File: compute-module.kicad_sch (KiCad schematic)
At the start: 99 parts, among them J1 DF40HC(3.0)-100DS-0.4v, J2 DF40HC(3.0)-100DS-0.4v, M1 compute-module-4-1.5mm

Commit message: [#54617] Review requested changes
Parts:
- removed R? (x4): 4x0R_0402_array, antmicro-footprints:4x0R_0402_array_EXB28V, symbol antmicroResistorNetworksArrays:4x0R_0402_array
- added R? (x15): R_0R_0402, antmicro-footprints:R_0402_1005Metric, symbol antmicroResistors0402:R_0R_0402
- added R?: R_100k_0402, antmicro-footprints:R_0402_1005Metric, symbol antmicroResistors0402:R_100k_0402
- D? (x2): MPN TPD1E0B04DPYR -> TPD1E0B04DPYR
- Q? (x2): Manufacturer Panjit -> PANJIT
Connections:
- net Exp.SCL: now also R?.2
- net Exp.SDA: now also R?.2
- net FT4233.SCL: now also R?.2
- net FT4233.SDA: now also R?.2
- net GND: now also R?.1; no longer J1.100, TP?.1
- net I_{2}C_CSI0.SCL: now also R?.2
- net I_{2}C_CSI0.SDA: now also R?.2
- net I_{2}C_LED.SCL: now also R?.2
- net I_{2}C_LED.SDA: now also R?.2
- net I_{2}C_Sensor.SCL: now also R?.2
- net I_{2}C_Sensor.SDA: now also R?.2
- net I_{2}C_{3V3}.SCL: now also R?.1, R?.1, R?.1, R?.1, R?.1, R?.1, R?.1
- net I_{2}C_{3V3}.SDA: now also R?.1, R?.1, R?.1, R?.1, R?.1, R?.1, R?.1
- net NFC.I_{2}C_SCL: now also R?.2
- net NFC.I_{2}C_SDA: now also R?.2
- net PolarfireID: now also R?.2
- net AntmUD.DIM renamed GPIO.18
- net GPIO.18: now also R?.2
- net AntmUD.EN renamed DSICtrl.EN
- net AntmUD.GPIO renamed DSICtrl.GPIO
- net AntmUD.IRQ1 renamed DSICtrl.IRQ1
- net AntmUD.~{IRQ2} renamed DSICtrl.~{IRQ2}
- net AntmUD.~{RST} renamed DSICtrl.~{RST}
- net NVMe.RX_N renamed NVMe.RX0_N
- net NVMe.RX_P renamed NVMe.RX0_P
- net NVMe.TX_N renamed NVMe.TX0_N
- net NVMe.TX_P renamed NVMe.TX0_P
- new net DSICtrl.DIM: R?.1
- new net DSICtrl.SCL: R?.2
- new net DSICtrl.SDA: R?.2
- new net nEXTRST: J1.100, TP?.1
- no-connect marks 16 -> 12
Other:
- note added: "Note: I_{2}C address selection: A2|A1|A0| write address 0 |0 |0 | 0x40 0 |0 |1 | 0x42 0 |1 |0 | 0x44 0 |1 |1 | 0x46 1 |0 |0 | 0x48 1 |0 |1 | 0x4A 1 |1 |0 | 0x4C 1 |1 |1 | 0x4E"
- note removed: "Note: I_{2}C address selection: A2|A1|A0| write address 0 |0 |0 | 0x40 0 |0 |1 | 0x41 0 |1 |0 | 0x42 0 |1 |1 | 0x43 1 |0 |0 | 0x44 1 |0 |1 | 0x45 1 |1 |0 | 0x46 1 |1 |1 | 0x47"
- moved on the sheet: R?

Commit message: [#54617] Re-enumerate reference designators
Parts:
- gave numbers to parts that had none: 104
- renumbered J1 to J201, J2 to J202, M1 to M201, SP1 to SP201, SP2 to SP202, SP3 to SP203, SP4 to SP204
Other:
- moved on the sheet: R238, R239

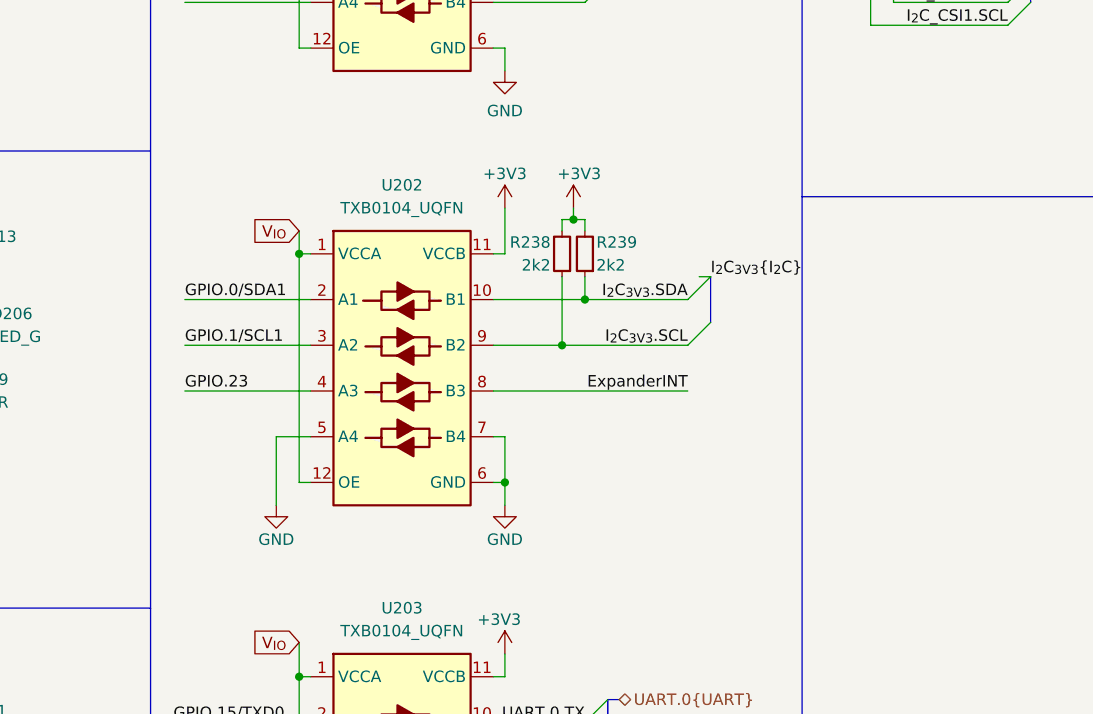
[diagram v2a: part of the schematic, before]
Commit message: [#54617] Change level shifter for I2C
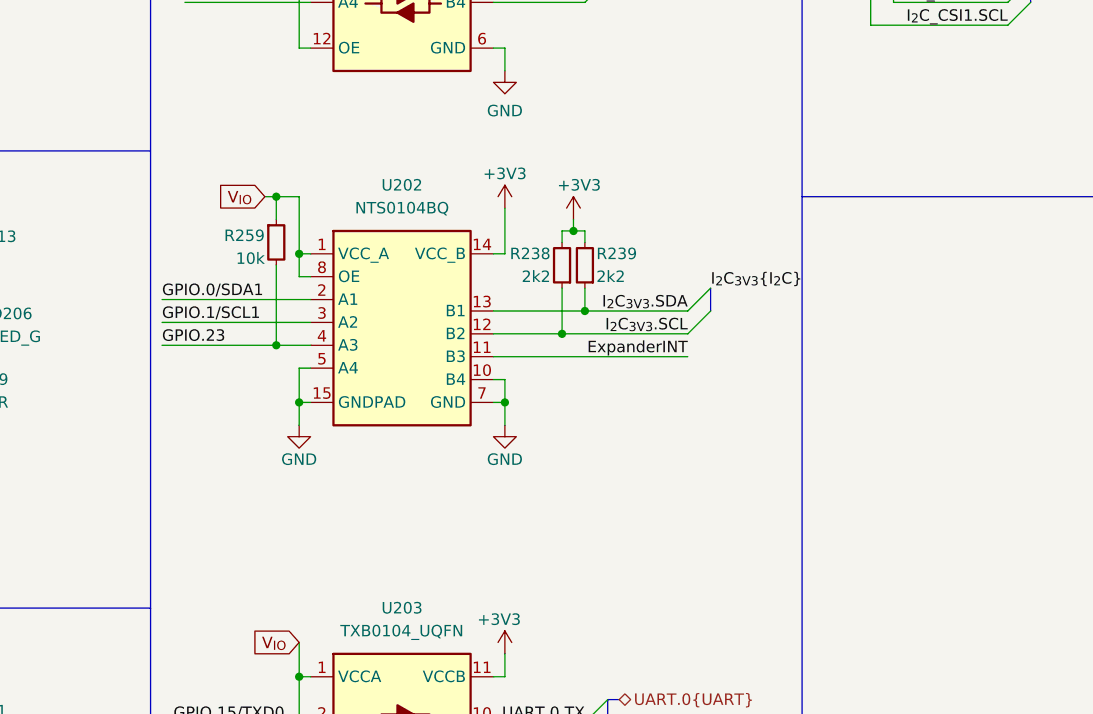
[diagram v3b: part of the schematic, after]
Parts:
- removed U202: TXB0104_UQFN, antmicro-footprints:UQFN-12_2x1.7mm_P0.4mm_Texas_RUT, symbol antmicroLogicTranslatorsLevelShifters:TXB0104_UQFN
- added R259: R_10k_0402, antmicro-footprints:R_0402_1005Metric, symbol antmicroResistors0402:R_10k_0402
- added U202: NTS0104_DHVQFN, antmicro-footprints:DHVQFN-14-1EP_2.5x3mm, symbol antmicroLogicTranslatorsLevelShifters:NTS0104_DHVQFN
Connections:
- net +3V3: now also U202.14 (VCC_B)
- net ExpanderINT: now also U202.11 (B3)
- net GND: now also U202.10 (B4), U202.15 (GNDPAD), U202.5 (A4), U202.7 (GND)
- net GPIO.0/SDA1: now also U202.2 (A1)
- net GPIO.1/SCL1: now also U202.3 (A2)
- net GPIO.23: now also R259.2, U202.4 (A3)
- net I_{2}C_{3V3}.SCL: now also U202.12 (B2)
- net I_{2}C_{3V3}.SDA: now also U202.13 (B1)
- net V_{IO}: now also R259.1, U202.1 (VCC_A), U202.8 (OE)
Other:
- moved on the sheet: R238, R239

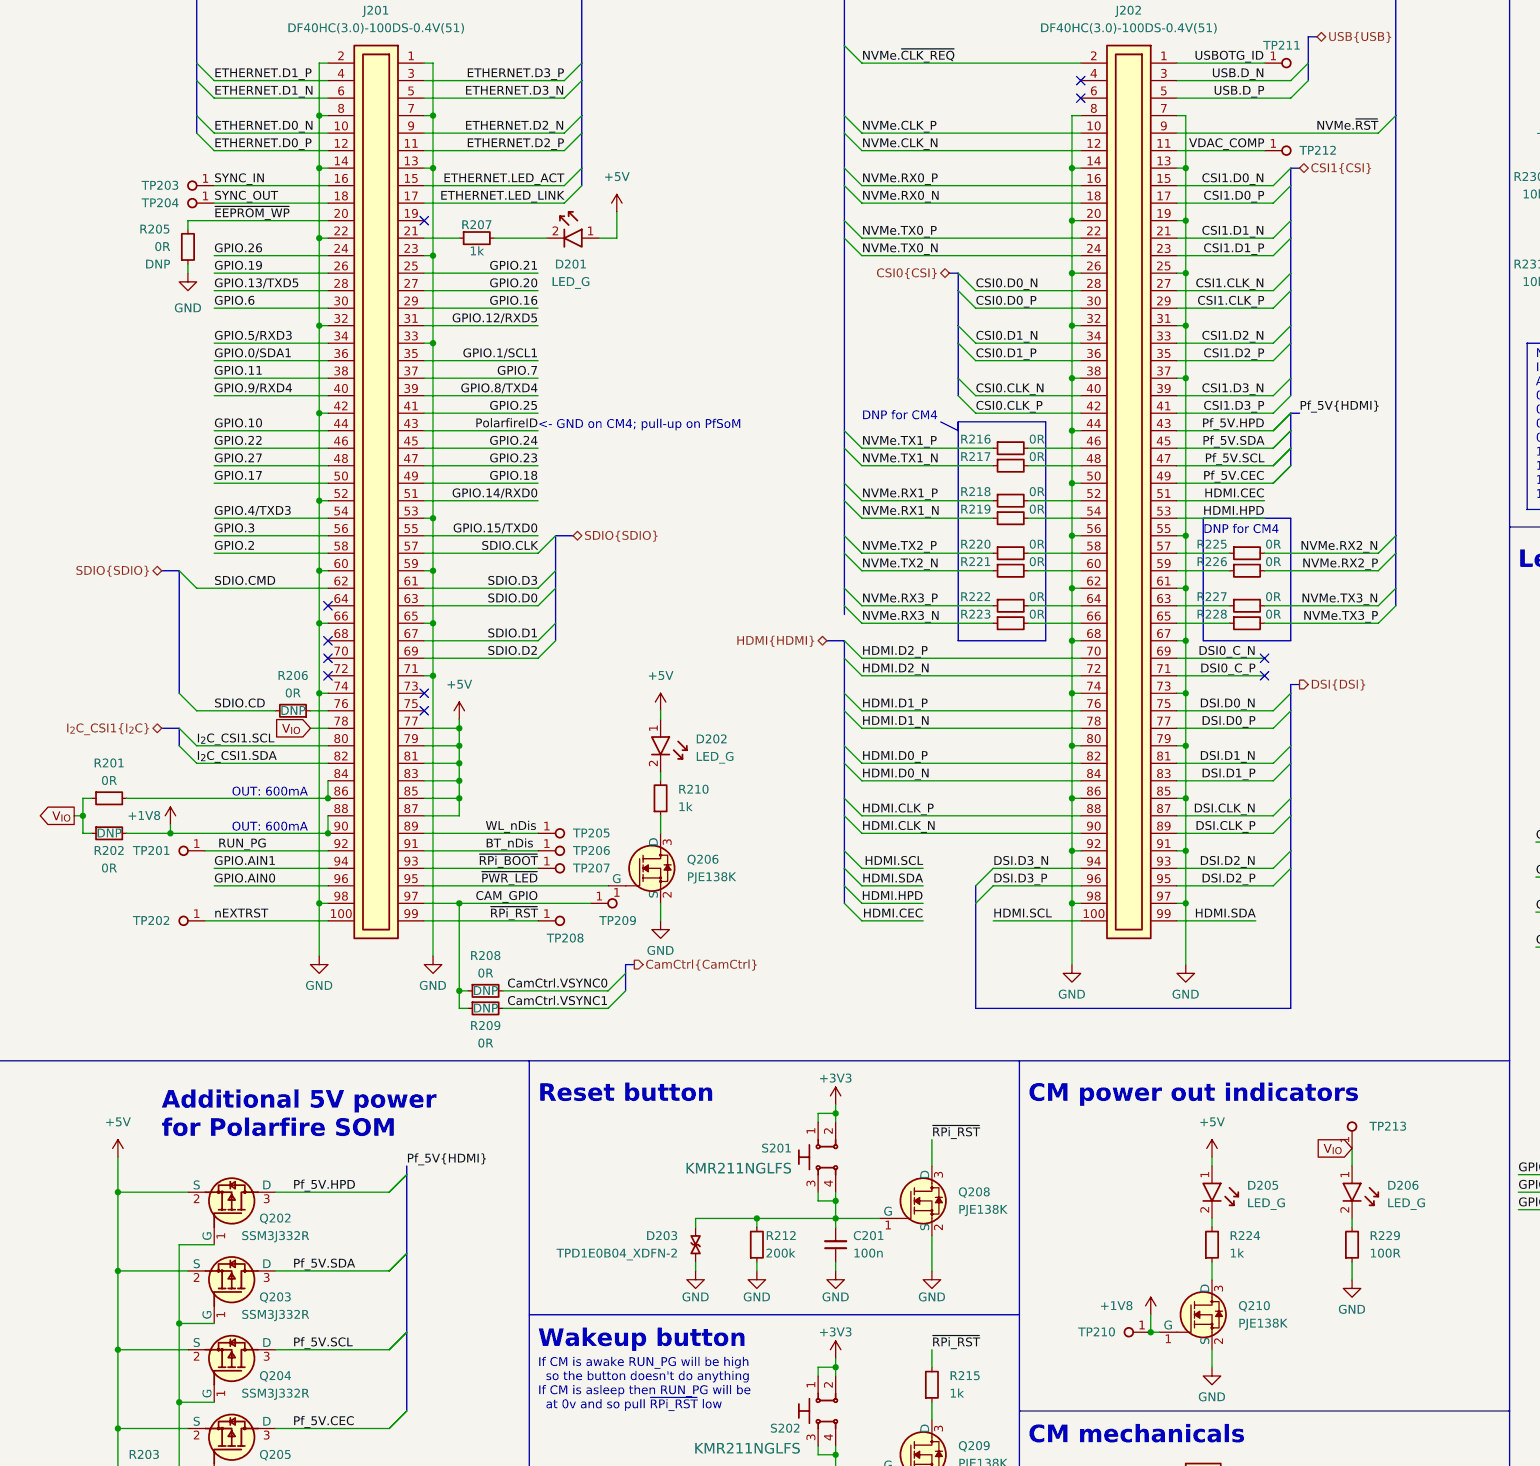
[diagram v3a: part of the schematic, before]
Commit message: [#55181] Rotate board; Change CSI&SD position; Update adapter; NFC placement
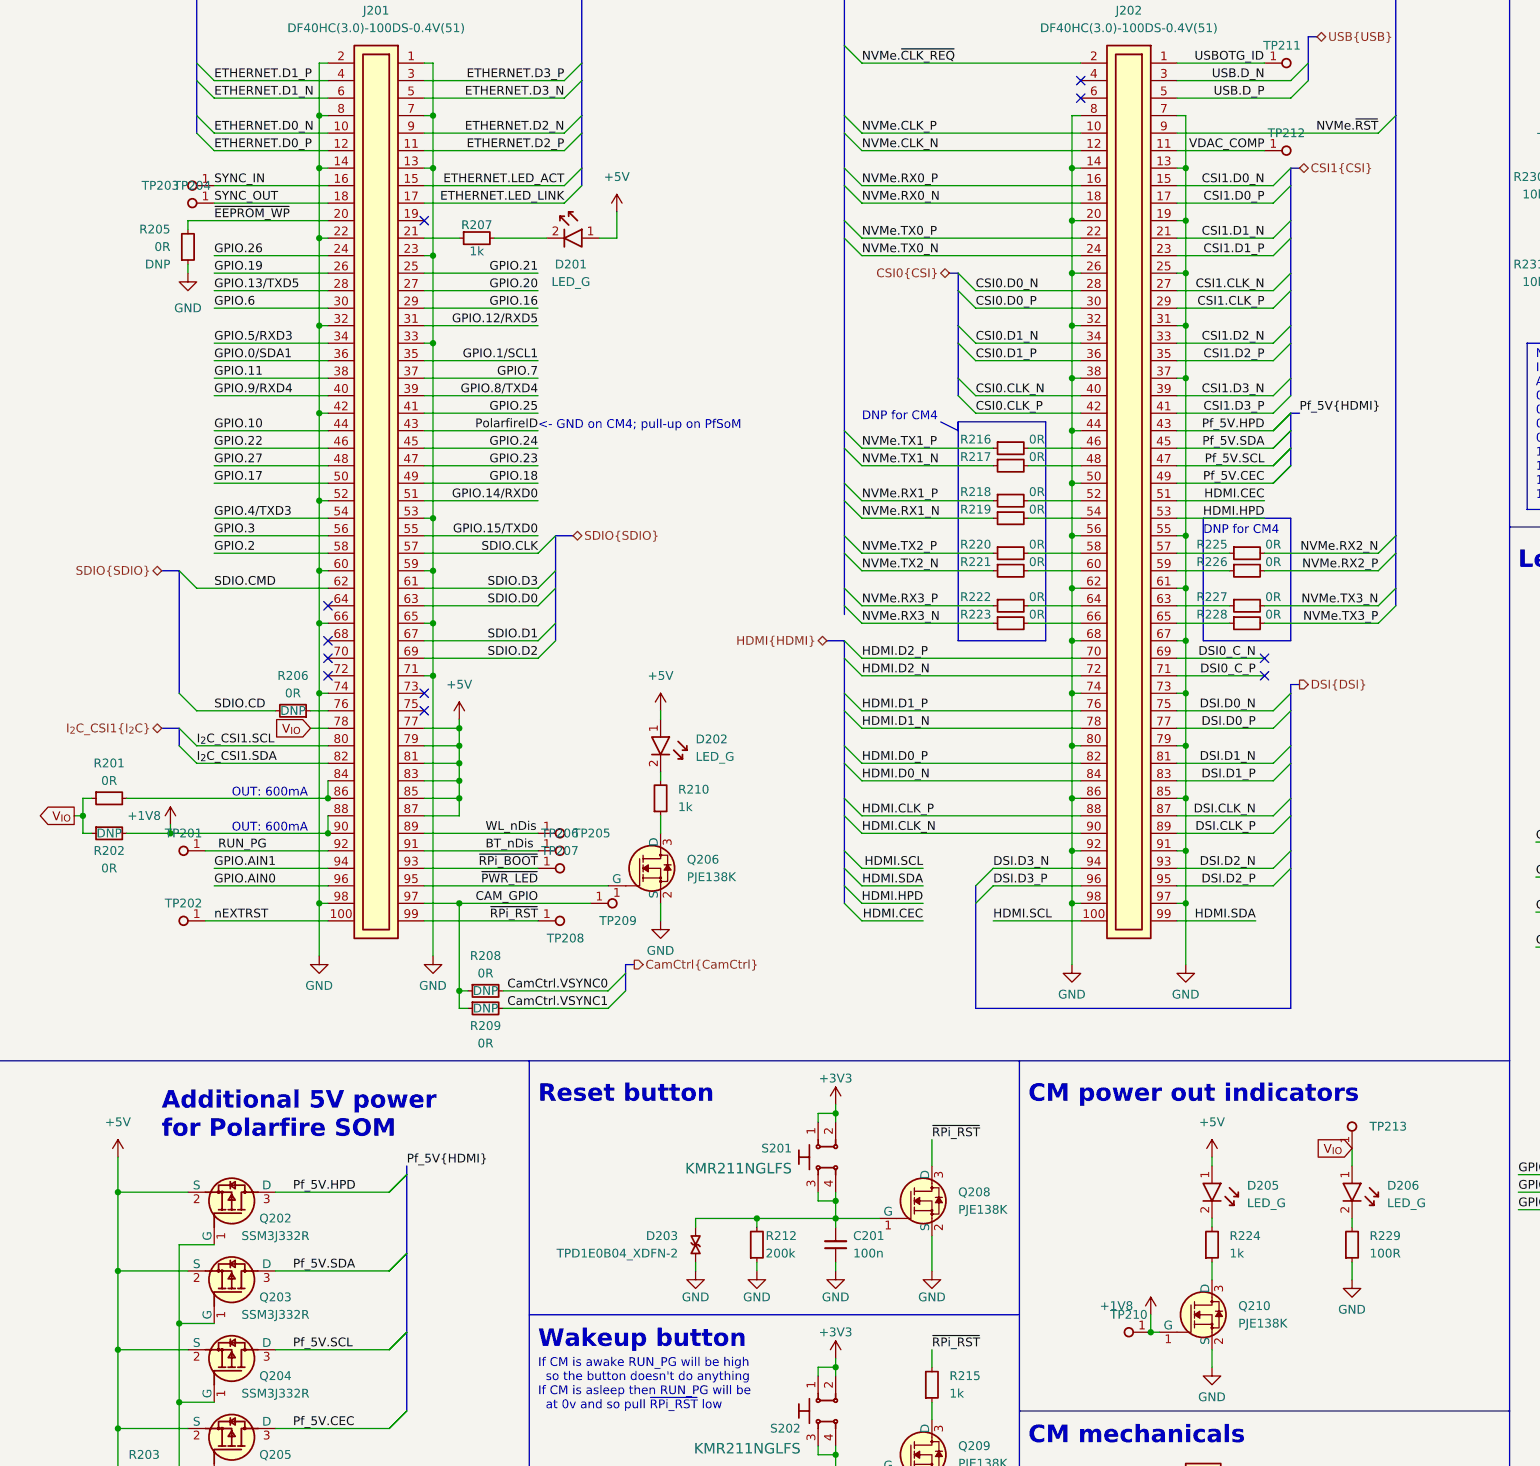
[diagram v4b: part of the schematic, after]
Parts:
- TP201, TP202, TP203, TP204, TP205, TP206, TP207, TP208, TP209, TP210, TP211, TP212, TP213: footprint antmicro-footprints:TP_SMD_1mm -> antmicro-footprints:TP_SMD_0.75mm; symbol antmicroTestPoints:TP_1mm_SMD -> antmicroTestPoints:TP_0.75mm_SMD; now left out of the parts list
